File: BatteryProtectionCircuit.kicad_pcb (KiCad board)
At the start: 2 copper layers, 55.5 x 44 mm, 41 parts, among them J2 Conn_01x07_Pin, Q1 NMOS, U2 LM358, U3 LM358, U4 LM321, U6 LMC555xN

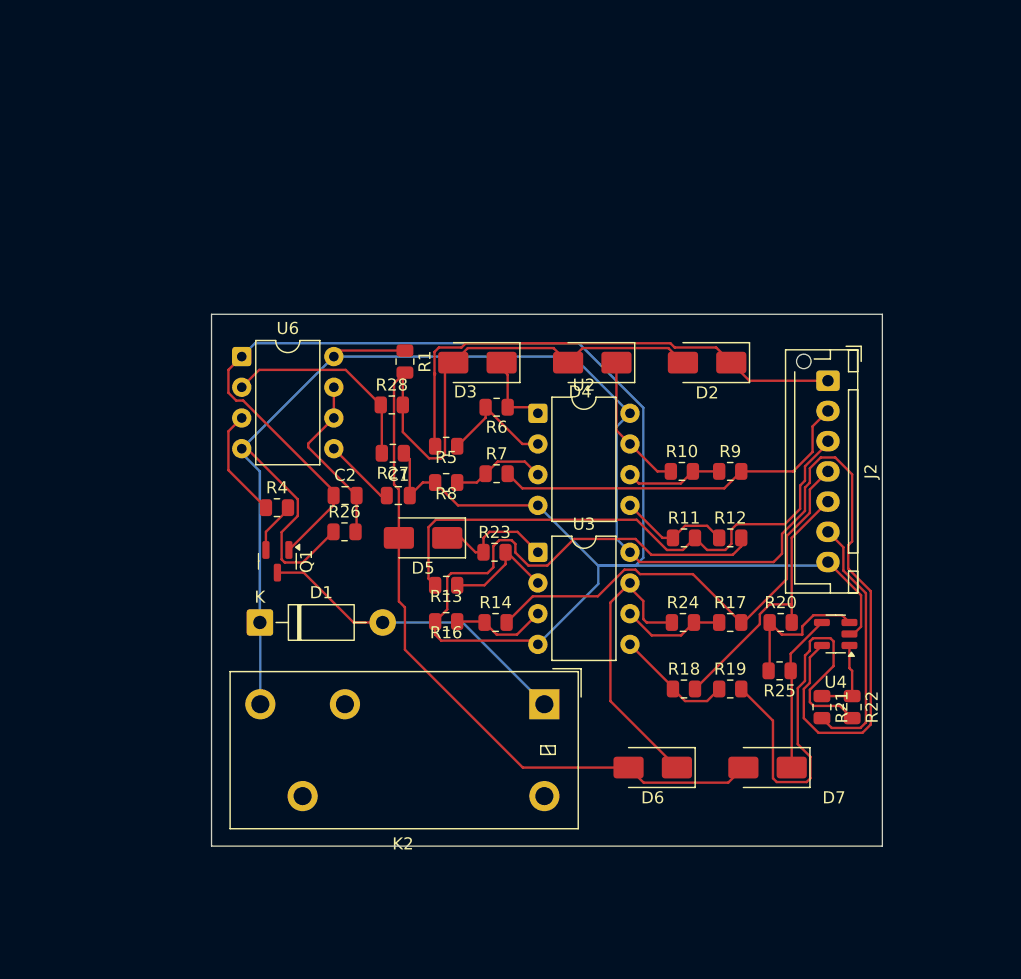
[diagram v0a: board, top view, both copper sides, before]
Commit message: Changes to routing
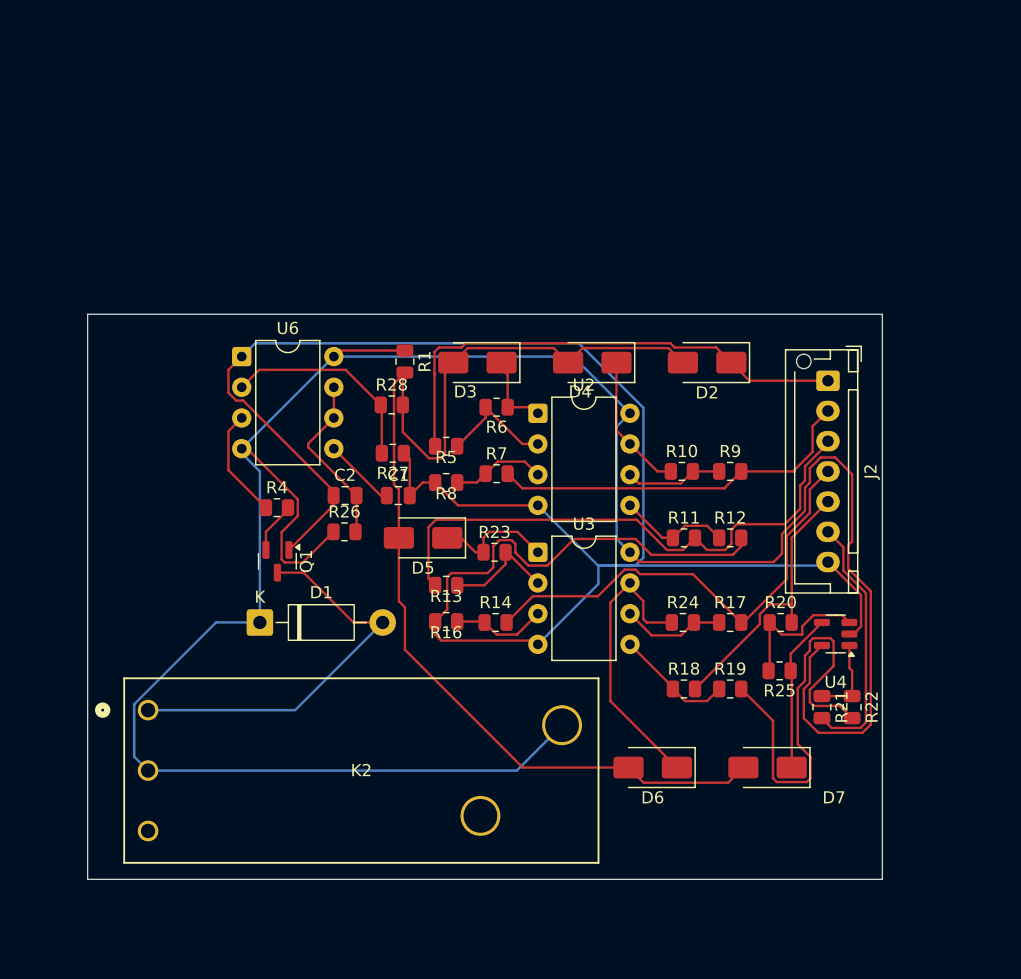
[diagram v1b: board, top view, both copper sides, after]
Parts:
- K2: footprint Relay_THT:Relay_SPDT_Panasonic_JW1_FormC -> New Relay:CONN5_21105_PAN
- moved K2 32.8 mm to (187.8, 143.2), turned to 0 degrees
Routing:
- net /VIN: track 155.1 -> 203.2 mm
- net /REL: track 26.6 -> 32.8 mm
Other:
- board size 55.5 x 44 mm -> 65.8 x 46.8 mm

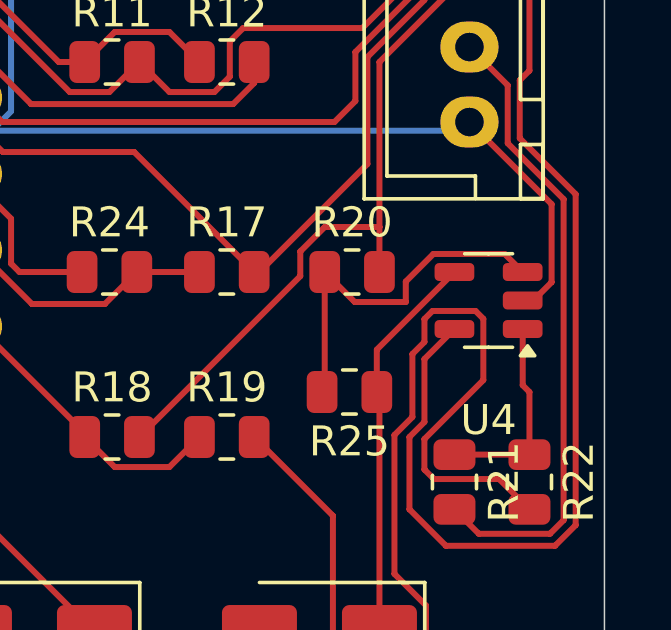
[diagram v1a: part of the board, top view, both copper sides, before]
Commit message: Added Connectors for power rail and robot input
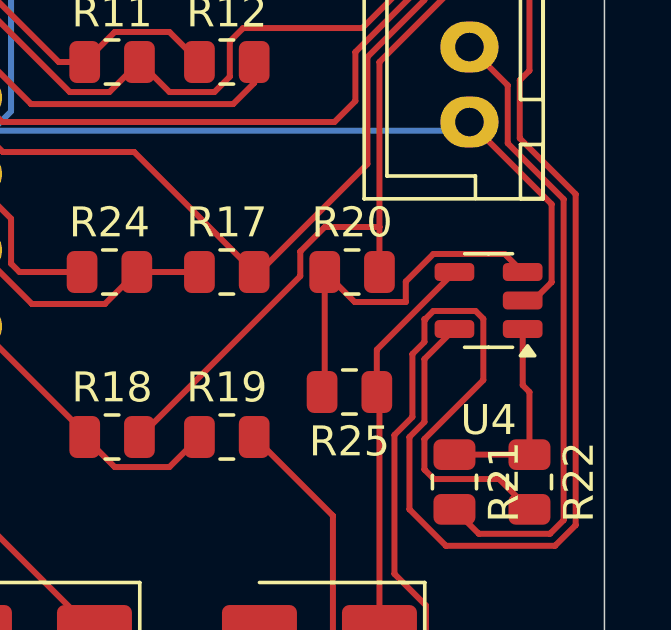
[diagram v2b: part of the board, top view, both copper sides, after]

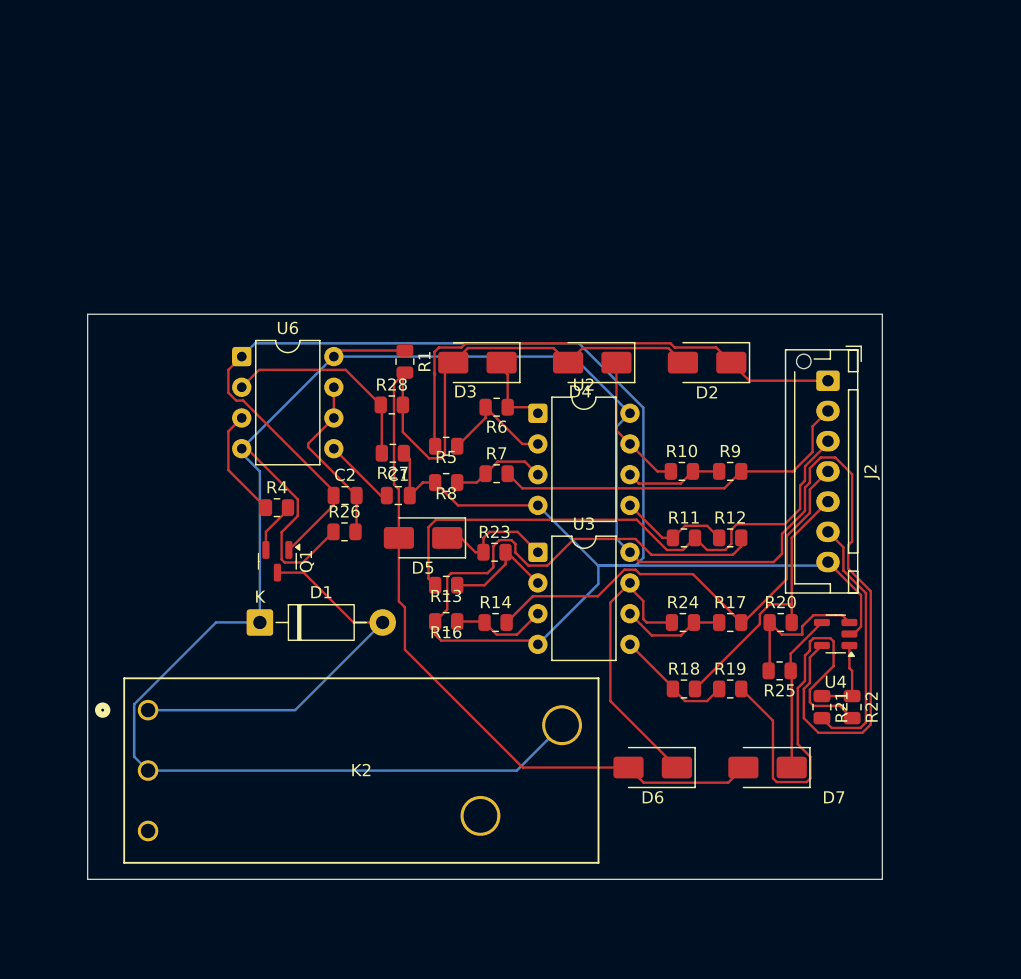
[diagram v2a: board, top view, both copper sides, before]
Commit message: Finalized(?) PCB tracing
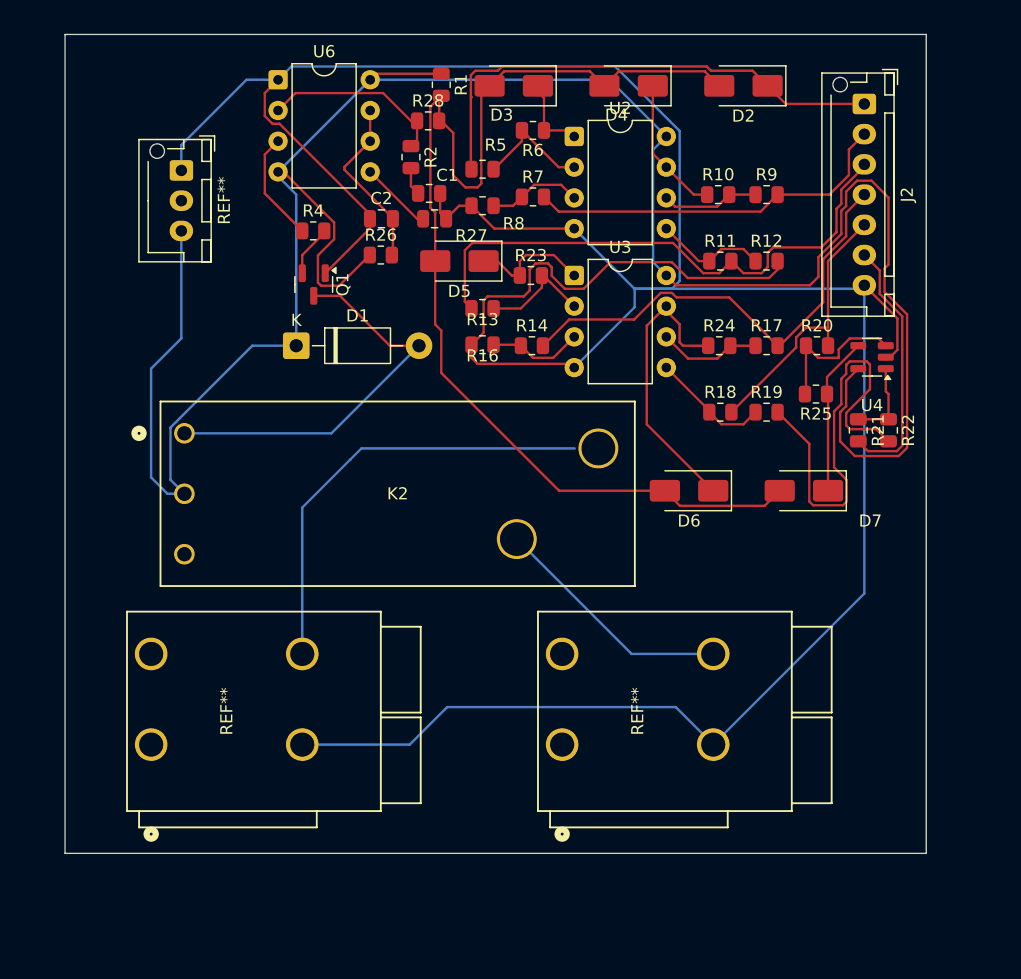
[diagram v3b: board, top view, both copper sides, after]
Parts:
- added R2: 62K, Resistor_SMD:R_0805_2012Metric, F.Cu at (209.5, 97.5)
- added REF**: JST_XH_B3B-XH-AM_1x03_P2.50mm_Vertical, Connector_JST:JST_XH_B3B-XH-AM_1x03_P2.50mm_Vertical, F.Cu at (190.5, 98.6)
- added REF**: CONN2_2606-1102_WAG, footprints:CONN2_2606-1102_WAG, F.Cu at (222.0, 146.1)
- added REF**: CONN2_2606-1102_WAG, footprints:CONN2_2606-1102_WAG, F.Cu at (188.0, 146.1)
- R27: value 200k -> 2.4K
- moved R28 23.7 mm to (210.9, 94.5)
- moved R5 23.1 mm to (215.4, 98.5)
- moved C1 23.1 mm to (211.5, 102.6)
- moved K2 23.1 mm to (190.8, 120.4)
- moved Q1 23.1 mm to (201.5, 108.0)
- moved C2 23.1 mm to (207.1, 102.6)
- moved D1 23.1 mm to (200.0, 113.1)
- moved D2 23.1 mm to (237.0, 91.6)
- moved D3 23.1 mm to (218.0, 91.6)
- moved D4 23.1 mm to (227.5, 91.6)
- moved D5 23.1 mm to (213.5, 106.1)
- moved D6 23.1 mm to (232.5, 125.1)
- moved D7 23.1 mm to (242.0, 125.1)
- moved J2 23.1 mm to (247.0, 93.1)
- moved R1 23.1 mm to (212.0, 91.5)
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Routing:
- net /GND: track 212.7 -> 303.9 mm
- net /VIN: track 203.2 -> 228.9 mm
- net OUT: track 9.16 -> 29.3 mm
- net /VD: track 95.1 -> 96.1 mm
- net /TR: track 17.3 -> 18.0 mm
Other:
- board size 65.8 x 46.8 mm -> 71.2 x 67.8 mm

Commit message: Updated Trace Widths
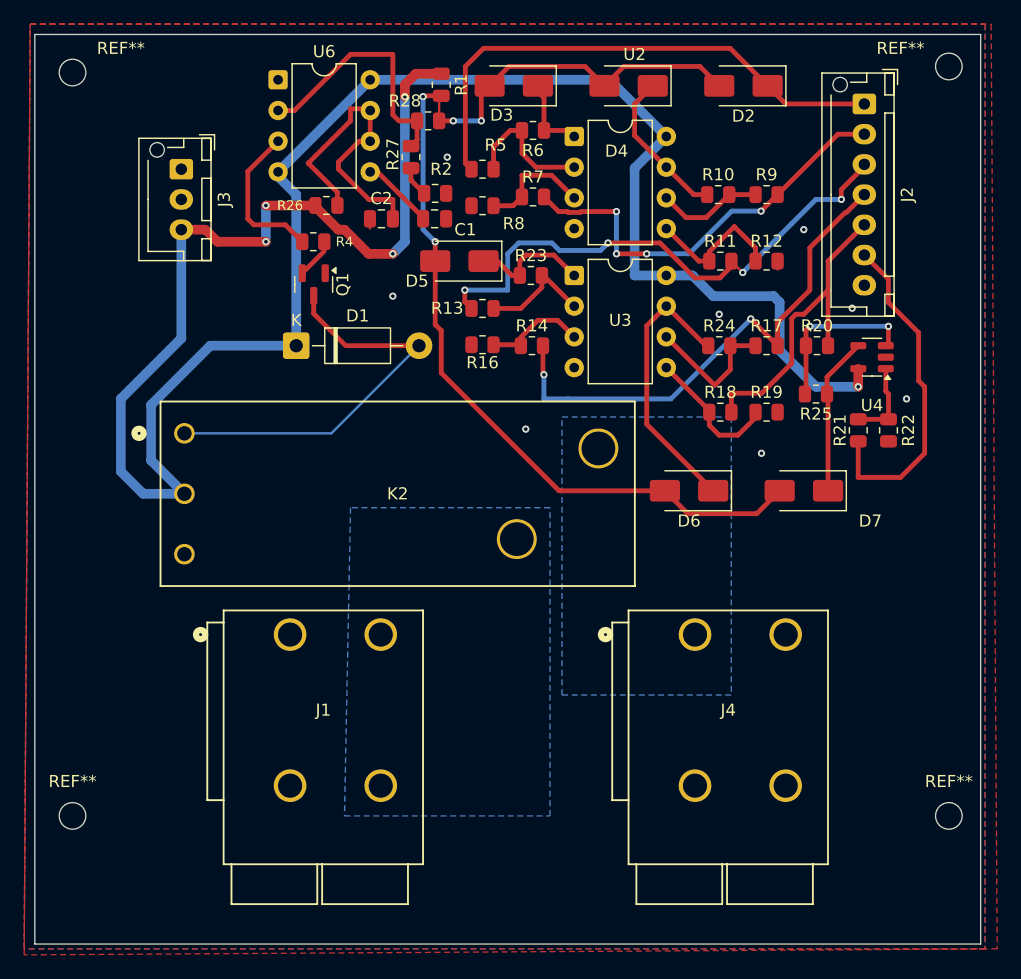
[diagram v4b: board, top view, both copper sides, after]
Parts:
- removed the REF** at (190.5, 98.6)
- removed the REF** at (222.0, 146.1)
- removed the REF** at (188.0, 146.1)
- added J1: Conn_01x04_Pin, footprints:CONN2_2606-1102_WAG, F.Cu at (199.5, 137.0)
- added J3: Conn_01x03_Pin, Connector_JST:JST_XH_B3B-XH-AM_1x03_P2.50mm_Vertical, F.Cu at (190.5, 98.5)
- added J4: Conn_01x04_Pin, footprints:CONN2_2606-1102_WAG, F.Cu at (233.0, 137.0)
- added REF**: MountingHole_2.2mm_M2_DIN965, MountingHole:MountingHole_2.2mm_M2_DIN965, F.Cu at (254.0, 90.0)
- added REF**: MountingHole_2.2mm_M2_DIN965, MountingHole:MountingHole_2.2mm_M2_DIN965, F.Cu at (254.0, 152.0)
- added REF**: MountingHole_2.2mm_M2_DIN965, MountingHole:MountingHole_2.2mm_M2_DIN965, F.Cu at (181.5, 90.5)
- added REF**: MountingHole_2.2mm_M2_DIN965, MountingHole:MountingHole_2.2mm_M2_DIN965, F.Cu at (181.5, 152.0)
- R2: value 62K -> 2.4k
- R27: value 2.4K -> 62k
- moved R26 6.09 mm to (202.5, 101.5)
- moved R2 3.61 mm to (211.5, 100.5), turned to 0 degrees
- moved R27 3.36 mm to (209.5, 97.5), turned to 90 degrees
- moved R4 0.90 mm to (201.4, 104.5)
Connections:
- C1 pad 2: /GND -> GND
- C2 pad 1: /GND -> GND
- J2 pad 7: /GND -> GND
- K2 pad 3: OUT -> /R_OUT
- K2 pad 4: /VIN -> /B_IN
- Q1 pad 1: /GND -> GND
- R12 pad 2: /GND -> GND
- R16 pad 2: /GND -> GND
- R19 pad 2: /GND -> GND
- R2 pad 1: /TR -> Net-(R2-Pad1)
- R2 pad 2: /TR -> GND
- R22 pad 2: /GND -> GND
- R27 pad 1: /GND -> Net-(R2-Pad1)
- R4 pad 1: OUT -> /OUT
- R8 pad 2: /GND -> GND
- U2 pad 4: /GND -> GND
- U3 pad 4: /GND -> GND
- U4 pad 2: /GND -> GND
- U6 pad 1: /GND -> GND
- U6 pad 3: OUT -> /OUT
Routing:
- net /GND: track 303.9 -> 0.00 mm
- net /VIN: track 228.9 -> 183.2 mm, vias 0 -> 5
- net OUT: track 29.3 -> 0.00 mm
- net /OUT: track 0.00 -> 12.8 mm
- net Net-(U6-DIS): track 14.5 -> 25.7 mm
- net /VD: track 96.1 -> 88.9 mm, vias 0 -> 4
- net /D52: track 21.2 -> 27.8 mm
- net /D32: track 38.6 -> 43.0 mm, vias 0 -> 2
- net /D42: track 22.6 -> 26.5 mm
- net /D12: track 30.9 -> 34.7 mm, vias 0 -> 4
- net /TR: track 18.0 -> 21.5 mm
- net GND: track 0.00 -> 3.24 mm, vias 0 -> 8
- net Net-(U3B--): track 8.57 -> 11.6 mm
- net Net-(U2B-+): track 9.32 -> 12.0 mm
- net Net-(R2-Pad1): track 0.00 -> 2.54 mm
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- added copper zone on B.Cu, net /B_IN
- added copper zone on B.Cu, net /R_OUT
- added copper zone on B.Cu, net GND
- added copper zone on F.Cu, net GND
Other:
- board size 71.2 x 67.8 mm -> 78.3 x 75.2 mm
